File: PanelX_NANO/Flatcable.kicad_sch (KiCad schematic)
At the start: 1 part

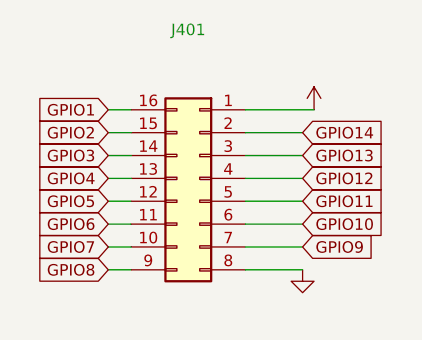
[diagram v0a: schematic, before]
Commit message: Deleted zip files from repo
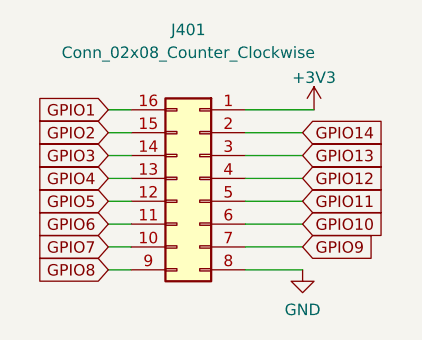
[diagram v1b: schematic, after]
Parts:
- J401: value (none) -> Conn_02x08_Counter_Clockwise; footprint (none) -> Connector_IDC:IDC-Header_2x08_P2.54mm_Vertical
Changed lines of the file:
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@@
       (effects (font (size 1.27 1.27)) hide)
     )
-    (property "Value" "" (id 1) (at 134.62 62.4642 0))
+    (property "Value" "+3V3" (id 1) (at 134.62 62.4642 0))
     (property "Footprint" "" (id 2) (at 134.62 66.04 0)
       (effects (font (size 1.27 1.27)) hide)
@@
       (effects (font (size 1.27 1.27)) hide)
     )
-    (property "Value" "" (id 1) (at 133.35 88.2634 0))
+    (property "Value" "GND" (id 1) (at 133.35 88.2634 0))
     (property "Footprint" "" (id 2) (at 133.35 83.82 0)
       (effects (font (size 1.27 1.27)) hide)
@@
     (in_bom yes) (on_board yes)
     (property "Reference" "J401" (id 0) (at 120.65 57.1531 0))
-    (property "Value" "" (id 1) (at 120.65 59.69 0))
-    (property "Footprint" "" (id 2) (at 121.92 73.66 0)
+    (property "Value" "Conn_02x08_Counter_Clockwise" (id 1) (at 120.65 59.69 0))
+    (property "Footprint" "Connector_IDC:IDC-Header_2x08_P2.54mm_Vertical" (id 2) (at 121.92 73.66 0)
       (effects (font (size 1.27 1.27)) hide)
     )
